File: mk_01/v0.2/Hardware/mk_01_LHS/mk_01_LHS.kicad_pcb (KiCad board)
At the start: 2 copper layers, 165.1 x 102.9 mm, 79 parts, among them SW1 SW_Push_Dual, U1 nice_nano

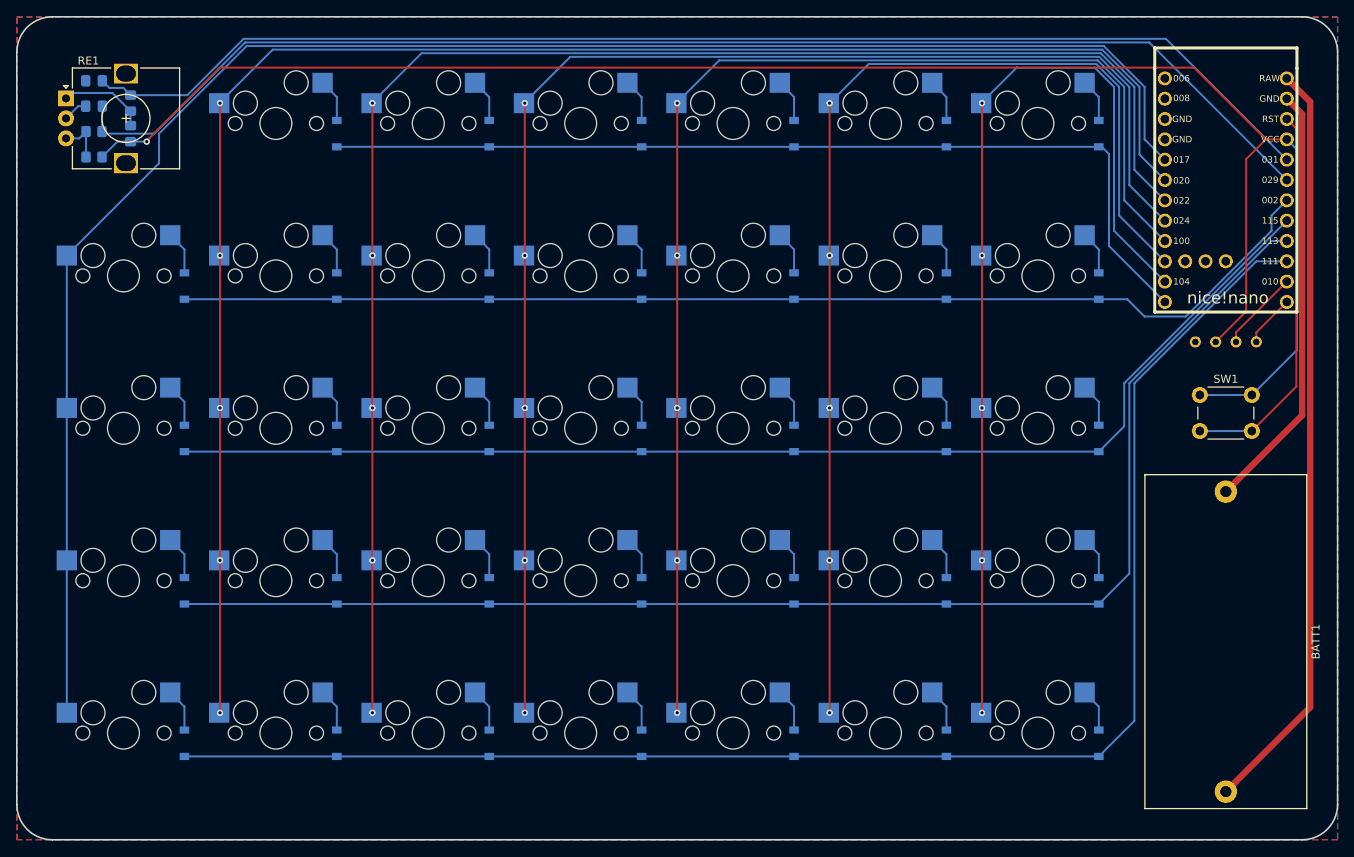
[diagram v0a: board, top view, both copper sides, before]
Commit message: Finalising layout and troubleshooting round-tracks
The layout is pretty much complete, with all necessary components wired correctly. round-tracks keeps refusing to round one of the traces. A label free version has been added, however I'll probably remove this since it means two designs to constantly keep up to date.
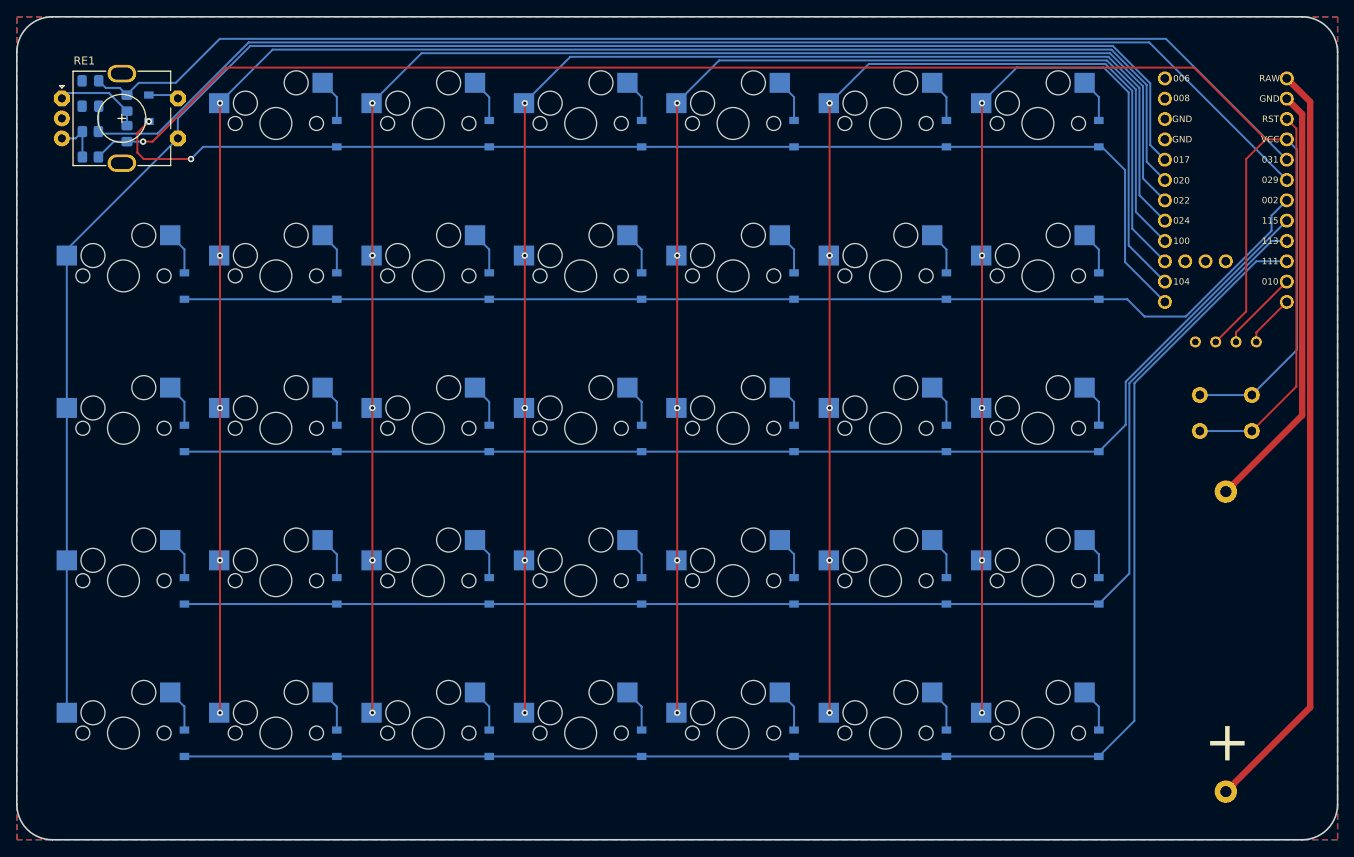
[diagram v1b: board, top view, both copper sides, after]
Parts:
- added D_35: D, Diode_SMD:D_SOD-123, B.Cu at (43.8, 45.1)
- RE1: value RotaryEncoder -> RotaryEncoder_Switch; footprint Rotary_Encoder:RotaryEncoder_Alps_EC12E_Vertical_H20mm -> Rotary_Encoder:RotaryEncoder_Alps_EC11E-Switch_Vertical_H20mm
- moved RE1 0.52 mm to (32.9, 43.9)
- moved C7 0.45 mm to (36.5, 41.7)
- moved C8 0.45 mm to (36.5, 44.8)
- moved R1 0.45 mm to (41.1, 44.5)
- moved R2 0.45 mm to (41.1, 48.3)
- moved R3 0.45 mm to (36.5, 48.0)
- moved R4 0.45 mm to (36.5, 51.2)
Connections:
- net Net-(C7-Pad2) renamed P0.31
- net Net-(C8-Pad1) renamed P0.29
- U1 pad 4: unconnected-(U1-Pad4) -> Earth
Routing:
- net row0: track 118.3 -> 148.7 mm, vias 0 -> 2
- net Net-(RE1-PadS2): track 0.00 -> 4.53 mm
- net Earth: track 3.10 -> 0.00 mm
- net col4: track 157.1 -> 157.8 mm
- net col6: track 122.6 -> 123.3 mm
- net col3: track 174.4 -> 175.1 mm
- net col5: track 139.8 -> 140.4 mm
- net col2: track 191.6 -> 192.3 mm
- net col1: track 208.9 -> 209.6 mm
- net col0: track 217.2 -> 217.8 mm
